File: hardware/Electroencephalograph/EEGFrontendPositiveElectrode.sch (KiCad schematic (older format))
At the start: 81 parts, among them J1 Conn_01x08_Male

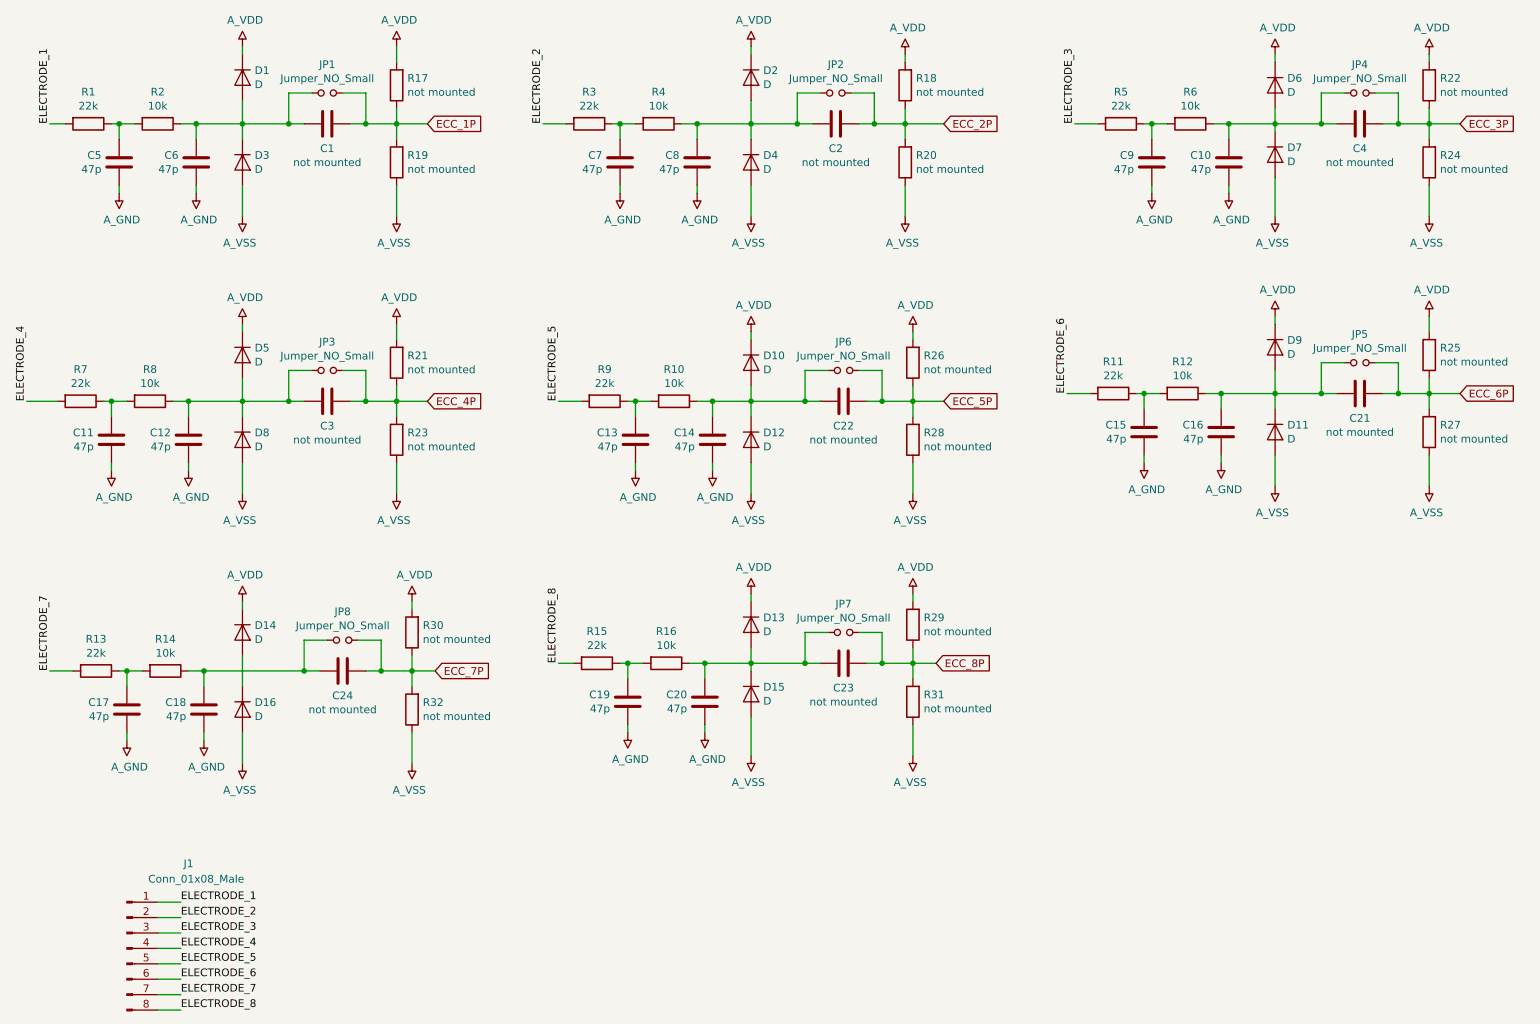
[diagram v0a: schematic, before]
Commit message: removed external clk and vref
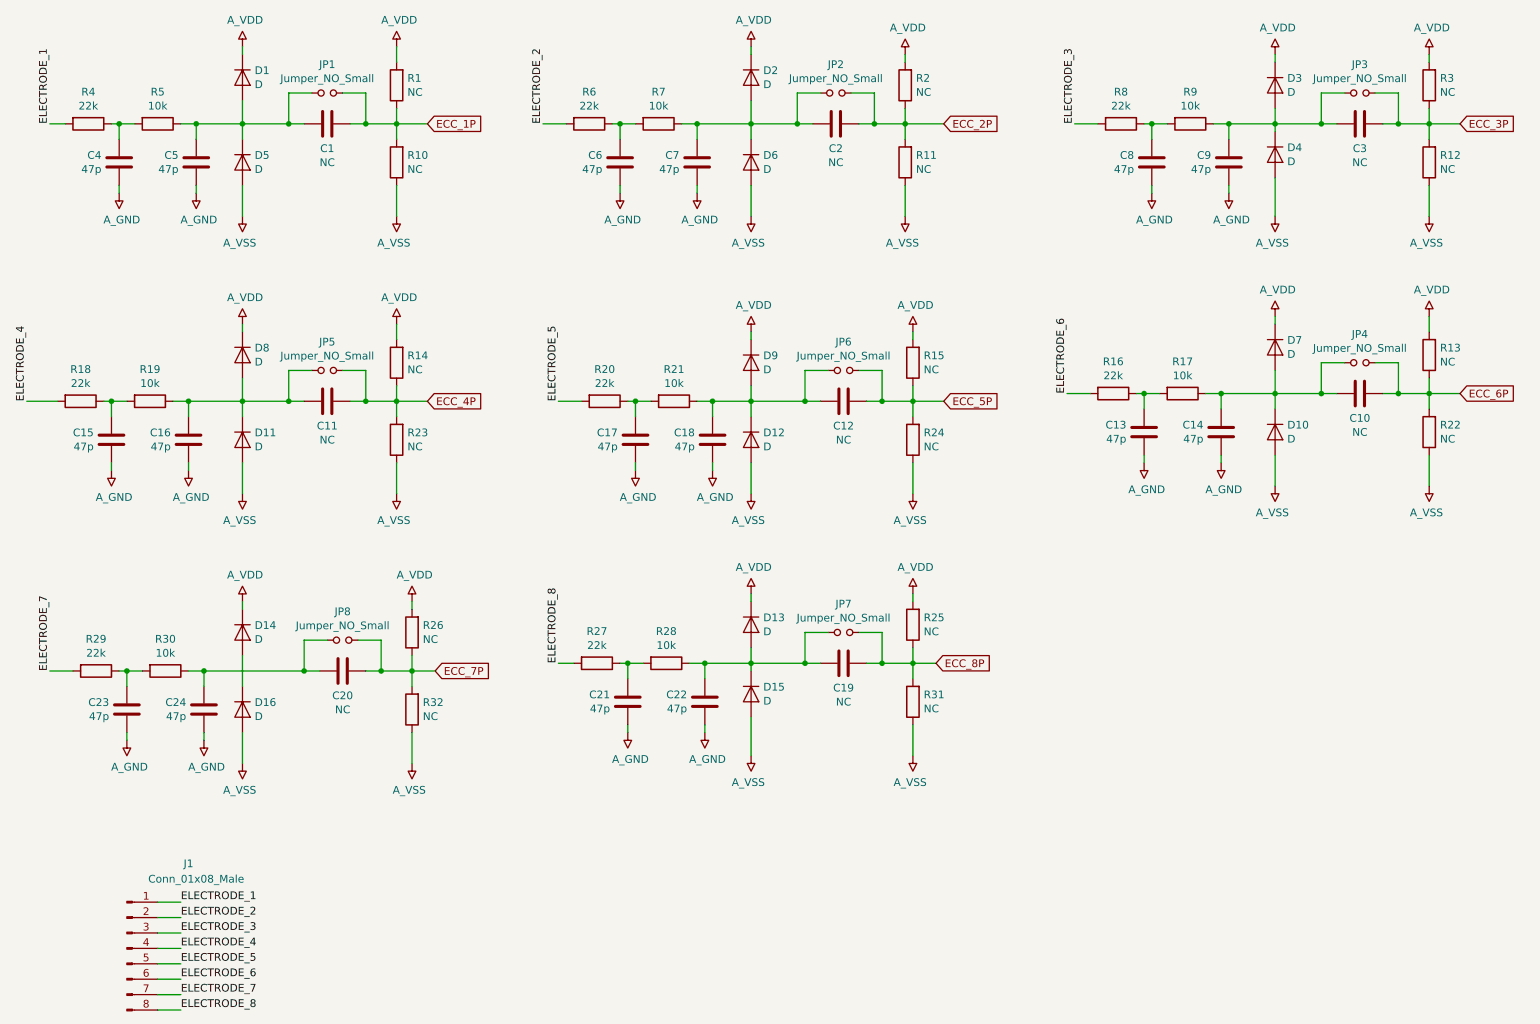
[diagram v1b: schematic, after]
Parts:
- C1, C2, R23, R31, R32: value not mounted -> NC
- C10: renamed from C21; value not mounted -> NC
- C11: renamed from C3; value not mounted -> NC
- C12: renamed from C22; value not mounted -> NC
- C19: renamed from C23; value not mounted -> NC
- C20: renamed from C24; value not mounted -> NC
- C3: renamed from C4; value not mounted -> NC
- R1: renamed from R17; value not mounted -> NC
- R10: renamed from R19; value not mounted -> NC
- R11: renamed from R20; value not mounted -> NC
- R12: renamed from R24; value not mounted -> NC
- R13: renamed from R25; value not mounted -> NC
- R14: renamed from R21; value not mounted -> NC
- R15: renamed from R26; value not mounted -> NC
- R2: renamed from R18; value not mounted -> NC
- R22: renamed from R27; value not mounted -> NC
- R24: renamed from R28; value not mounted -> NC
- R25: renamed from R29; value not mounted -> NC
- R26: renamed from R30; value not mounted -> NC
- R3: renamed from R22; value not mounted -> NC
- renumbered C15 to C13, C16 to C14, C11 to C15, C12 to C16, C13 to C17, C14 to C18, C19 to C21, C20 to C22, C17 to C23, C18 to C24, C5 to C4, C6 to C5, C7 to C6, C8 to C7, C9 to C8, C10 to C9, D11 to D10, D8 to D11, D6 to D3, D7 to D4, D3 to D5, D4 to D6, D9 to D7, D5 to D8, D10 to D9, JP4 to JP3, JP5 to JP4, JP3 to JP5, R11 to R16, R12 to R17, R7 to R18, R8 to R19, R9 to R20, R10 to R21, R15 to R27, R16 to R28, R13 to R29, R14 to R30, R1 to R4, R2 to R5, R3 to R6, R4 to R7, R5 to R8, R6 to R9
